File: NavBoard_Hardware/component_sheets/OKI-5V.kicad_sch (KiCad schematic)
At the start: 4 parts

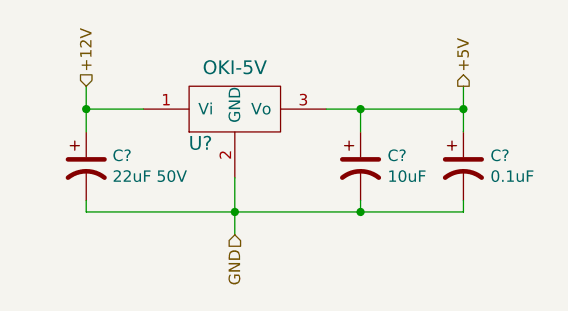
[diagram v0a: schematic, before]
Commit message: Created adapter symbols and footprints
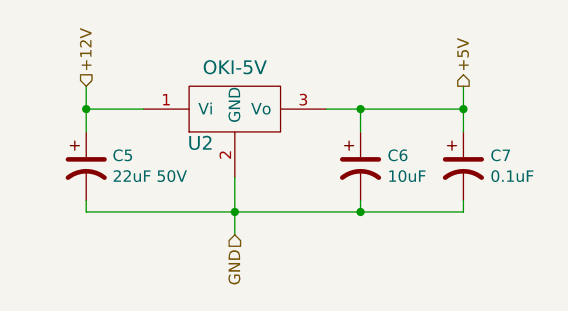
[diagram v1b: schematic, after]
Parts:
- gave numbers to parts that had none: 4
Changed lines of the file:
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@@
   (symbol (lib_id "Device:C_Polarized_US") (at 127.635 97.155 0) (unit 1)
     (in_bom yes) (on_board yes)
-    (property "Reference" "C?" (id 0) (at 130.556 95.9866 0)
+    (property "Reference" "C5" (id 0) (at 130.556 95.9866 0)
       (effects (font (size 1.27 1.27)) (justify left))
     )
@@
   (symbol (lib_id "Device:C_Polarized_US") (at 158.115 97.155 0) (unit 1)
     (in_bom yes) (on_board yes)
-    (property "Reference" "C?" (id 0) (at 161.1122 95.9866 0)
+    (property "Reference" "C6" (id 0) (at 161.1122 95.9866 0)
       (effects (font (size 1.27 1.27)) (justify left))
     )
@@
   (symbol (lib_id "Device:C_Polarized_US") (at 169.545 97.155 0) (unit 1)
     (in_bom yes) (on_board yes)
-    (property "Reference" "C?" (id 0) (at 172.5422 95.9866 0)
+    (property "Reference" "C7" (id 0) (at 172.5422 95.9866 0)
       (effects (font (size 1.27 1.27)) (justify left))
     )
@@
   (symbol (lib_id "MRDT_Devices:OKI") (at 139.065 93.345 0) (unit 1)
     (in_bom yes) (on_board yes)
-    (property "Reference" "U?" (id 0) (at 140.335 94.615 0)
+    (property "Reference" "U2" (id 0) (at 140.335 94.615 0)
       (effects (font (size 1.524 1.524)))
     )

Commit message: Added connectors, cleaned up file directory
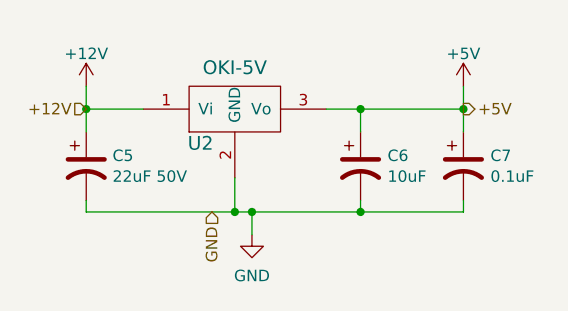
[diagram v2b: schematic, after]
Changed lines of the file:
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@@
     (comment 2 "Provides Stable 5V From 12V Input")
+  )
+  (junction (at 146.05 102.235) (diameter 0) (color 0 0 0 0)
   )
   (junction (at 158.115 102.235) (diameter 0) (color 0 0 0 0)
@@
   )
   (junction (at 169.545 90.805) (diameter 0) (color 0 0 0 0)
+  )
+  (wire (pts (xy 146.05 102.235) (xy 158.115 102.235))
+    (stroke (width 0) (type default) (color 0 0 0 0))
   )
   (wire (pts (xy 127.635 88.265) (xy 127.635 90.805))
@@
     (stroke (width 0) (type default) (color 0 0 0 0))
   )
-  (wire (pts (xy 144.145 102.235) (xy 158.115 102.235))
+  (wire (pts (xy 144.145 102.235) (xy 146.05 102.235))
     (stroke (width 0) (type default) (color 0 0 0 0))
   )
-  (wire (pts (xy 144.145 102.235) (xy 144.145 104.775))
+  (wire (pts (xy 146.05 102.235) (xy 146.05 104.775))
     (stroke (width 0) (type default) (color 0 0 0 0))
   )
@@
     (stroke (width 0) (type default) (color 0 0 0 0))
   )
-  (hierarchical_label "GND" (shape input) (at 144.145 104.775 270)
+  (hierarchical_label "GND" (shape input) (at 141.605 102.235 270)
     (effects (font (size 1.27 1.27)) (justify right))
   )
-  (hierarchical_label "+5V" (shape output) (at 169.545 88.265 90)
+  (hierarchical_label "+5V" (shape output) (at 169.545 90.805 0)
     (effects (font (size 1.27 1.27)) (justify left))
   )
-  (hierarchical_label "+12V" (shape input) (at 127.635 88.265 90)
-    (effects (font (size 1.27 1.27)) (justify left))
+  (hierarchical_label "+12V" (shape input) (at 127.635 90.805 180)
+    (effects (font (size 1.27 1.27)) (justify right))
   )
   (symbol (lib_id "Device:C_Polarized_US") (at 127.635 97.155 0) (unit 1)
@@
     (pin "1")
     (pin "2")
+  )
+  (symbol (lib_id "power:+5V") (at 169.545 88.265 0) (unit 1)
+    (in_bom yes) (on_board yes) (fields_autoplaced)
+    (property "Reference" "#PWR?" (id 0) (at 169.545 92.075 0)
+      (effects (font (size 1.27 1.27)) hide)
+    )
+    (property "Value" "+5V" (id 1) (at 169.545 84.6605 0))
+    (property "Footprint" "" (id 2) (at 169.545 88.265 0)
+      (effects (font (size 1.27 1.27)) hide)
+    )
+    (property "Datasheet" "" (id 3) (at 169.545 88.265 0)
+      (effects (font (size 1.27 1.27)) hide)
+    )
+    (pin "1")
+  )
+  (symbol (lib_id "power:+12V") (at 127.635 88.265 0) (unit 1)
+    (in_bom yes) (on_board yes) (fields_autoplaced)
+    (property "Reference" "#PWR?" (id 0) (at 127.635 92.075 0)
+      (effects (font (size 1.27 1.27)) hide)
+    )
+    (property "Value" "+12V" (id 1) (at 127.635 84.6605 0))
+    (property "Footprint" "" (id 2) (at 127.635 88.265 0)
+      (effects (font (size 1.27 1.27)) hide)
+    )
+    (property "Datasheet" "" (id 3) (at 127.635 88.265 0)
+      (effects (font (size 1.27 1.27)) hide)
+    )
+    (pin "1")
   )
   (symbol (lib_id "Device:C_Polarized_US") (at 169.545 97.155 0) (unit 1)
@@
     (pin "3")
   )
+  (symbol (lib_id "power:GND") (at 146.05 104.775 0) (unit 1)
+    (in_bom yes) (on_board yes) (fields_autoplaced)
+    (property "Reference" "#PWR?" (id 0) (at 146.05 111.125 0)
+      (effects (font (size 1.27 1.27)) hide)
+    )
+    (property "Value" "GND" (id 1) (at 146.05 109.3375 0))
+    (property "Footprint" "" (id 2) (at 146.05 104.775 0)
+      (effects (font (size 1.27 1.27)) hide)
+    )
+    (property "Datasheet" "" (id 3) (at 146.05 104.775 0)
+      (effects (font (size 1.27 1.27)) hide)
+    )
+    (pin "1")
+  )
 )

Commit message: Placed OKI SMD components, aligned ethernet pins
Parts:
- C5: footprint Capacitor_THT:CP_Radial_D6.3mm_P2.50mm -> Capacitor_SMD:C_1206_3216Metric_Pad1.33x1.80mm_HandSolder
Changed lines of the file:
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@@
       (effects (font (size 1.27 1.27)) (justify left))
     )
-    (property "Footprint" "Capacitor_THT:CP_Radial_D6.3mm_P2.50mm" (id 2) (at 127.635 97.155 0)
+    (property "Footprint" "Capacitor_SMD:C_1206_3216Metric_Pad1.33x1.80mm_HandSolder" (id 2) (at 127.635 97.155 0)
       (effects (font (size 1.27 1.27)) hide)
     )

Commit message: Annotated schematic pages
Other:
- company: Missouri S&T Mars Rover Design Team -> Thomas Francois, Missouri S&T Mars Rover Design Team
- title: OKI 5V Voltage Regulator -> MRDT NavBoard
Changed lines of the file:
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@@
   (paper "A4")
   (title_block
-    (title "OKI 5V Voltage Regulator")
-    (company "Missouri S&T Mars Rover Design Team")
+    (title "MRDT NavBoard")
+    (rev "1, 2023")
+    (company "Thomas Francois, Missouri S&T Mars Rover Design Team")
     (comment 1 "OKI 5V Voltage Regulator")
-    (comment 2 "Provides Stable 5V From 12V Input")
+    (comment 2 "Provides stable 5V from 12V input")
   )
   (junction (at 146.05 102.235) (diameter 0) (color 0 0 0 0)

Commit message: Rearranged schematic
I realize now that this is a dumb idea...
Going to redesign the board so the teensy just sits on top
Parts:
- renumbered C5 to C?, C6 to C?, C7 to C?, U2 to U?
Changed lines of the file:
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@@
     (effects (font (size 1.27 1.27)) (justify right))
   )
-  (symbol (lib_id "Device:C_Polarized_US") (at 127.635 97.155 0) (unit 1)
+  (symbol (lib_id "Device:C_Polarized_US") (at 127.635 97.155 0)
     (in_bom yes) (on_board yes)
-    (property "Reference" "C5" (id 0) (at 130.556 95.9866 0)
+    (property "Reference" "C?" (id 0) (at 130.556 95.9866 0)
       (effects (font (size 1.27 1.27)) (justify left))
     )
@@
     (pin "2")
   )
-  (symbol (lib_id "Device:C_Polarized_US") (at 158.115 97.155 0) (unit 1)
+  (symbol (lib_id "Device:C_Polarized_US") (at 158.115 97.155 0)
     (in_bom yes) (on_board yes)
-    (property "Reference" "C6" (id 0) (at 161.1122 95.9866 0)
+    (property "Reference" "C?" (id 0) (at 161.1122 95.9866 0)
       (effects (font (size 1.27 1.27)) (justify left))
     )
@@
     (pin "2")
   )
-  (symbol (lib_id "power:+5V") (at 169.545 88.265 0) (unit 1)
+  (symbol (lib_id "power:+5V") (at 169.545 88.265 0)
     (in_bom yes) (on_board yes) (fields_autoplaced)
-    (property "Reference" "#PWR011" (id 0) (at 169.545 92.075 0)
+    (property "Reference" "#PWR?" (id 0) (at 169.545 92.075 0)
       (effects (font (size 1.27 1.27)) hide)
     )
@@
     (pin "1")
   )
-  (symbol (lib_id "power:+12V") (at 127.635 88.265 0) (unit 1)
+  (symbol (lib_id "power:+12V") (at 127.635 88.265 0)
     (in_bom yes) (on_board yes) (fields_autoplaced)
-    (property "Reference" "#PWR010" (id 0) (at 127.635 92.075 0)
+    (property "Reference" "#PWR?" (id 0) (at 127.635 92.075 0)
       (effects (font (size 1.27 1.27)) hide)
     )
@@
     (pin "1")
   )
-  (symbol (lib_id "Device:C_Polarized_US") (at 169.545 97.155 0) (unit 1)
+  (symbol (lib_id "Device:C_Polarized_US") (at 169.545 97.155 0)
     (in_bom yes) (on_board yes)
-    (property "Reference" "C7" (id 0) (at 172.5422 95.9866 0)
+    (property "Reference" "C?" (id 0) (at 172.5422 95.9866 0)
       (effects (font (size 1.27 1.27)) (justify left))
     )
@@
     (pin "2")
   )
-  (symbol (lib_id "MRDT_Devices:OKI") (at 139.065 93.345 0) (unit 1)
+  (symbol (lib_id "MRDT_Devices:OKI") (at 139.065 93.345 0)
     (in_bom yes) (on_board yes)
-    (property "Reference" "U2" (id 0) (at 140.335 94.615 0)
+    (property "Reference" "U?" (id 0) (at 140.335 94.615 0)
       (effects (font (size 1.524 1.524)))
     )
@@
     (pin "3")
   )
-  (symbol (lib_id "power:GND") (at 146.05 104.775 0) (unit 1)
+  (symbol (lib_id "power:GND") (at 146.05 104.775 0)
     (in_bom yes) (on_board yes) (fields_autoplaced)
-    (property "Reference" "#PWR012" (id 0) (at 146.05 111.125 0)
+    (property "Reference" "#PWR?" (id 0) (at 146.05 111.125 0)
       (effects (font (size 1.27 1.27)) hide)
     )

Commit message: Decided on pcb layout
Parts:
- U?: footprint MRDT_Devices:OKI_Horizontal -> Converter_DCDC:Converter_DCDC_Murata_OKI-78SR_Vertical
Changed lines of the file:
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@@
     (effects (font (size 1.27 1.27)) (justify right))
   )
-  (symbol (lib_id "Device:C_Polarized_US") (at 127.635 97.155 0)
+  (symbol (lib_id "Device:C_Polarized_US") (at 127.635 97.155 0) (unit 1)
     (in_bom yes) (on_board yes)
     (property "Reference" "C?" (id 0) (at 130.556 95.9866 0)
@@
     (pin "2")
   )
-  (symbol (lib_id "Device:C_Polarized_US") (at 158.115 97.155 0)
+  (symbol (lib_id "Device:C_Polarized_US") (at 158.115 97.155 0) (unit 1)
     (in_bom yes) (on_board yes)
     (property "Reference" "C?" (id 0) (at 161.1122 95.9866 0)
@@
     (pin "2")
   )
-  (symbol (lib_id "power:+5V") (at 169.545 88.265 0)
+  (symbol (lib_id "power:+5V") (at 169.545 88.265 0) (unit 1)
     (in_bom yes) (on_board yes) (fields_autoplaced)
-    (property "Reference" "#PWR?" (id 0) (at 169.545 92.075 0)
+    (property "Reference" "#PWR0123" (id 0) (at 169.545 92.075 0)
       (effects (font (size 1.27 1.27)) hide)
     )
@@
     (pin "1")
   )
-  (symbol (lib_id "power:+12V") (at 127.635 88.265 0)
+  (symbol (lib_id "power:+12V") (at 127.635 88.265 0) (unit 1)
     (in_bom yes) (on_board yes) (fields_autoplaced)
-    (property "Reference" "#PWR?" (id 0) (at 127.635 92.075 0)
+    (property "Reference" "#PWR0122" (id 0) (at 127.635 92.075 0)
       (effects (font (size 1.27 1.27)) hide)
     )
@@
     (pin "1")
   )
-  (symbol (lib_id "Device:C_Polarized_US") (at 169.545 97.155 0)
+  (symbol (lib_id "Device:C_Polarized_US") (at 169.545 97.155 0) (unit 1)
     (in_bom yes) (on_board yes)
     (property "Reference" "C?" (id 0) (at 172.5422 95.9866 0)
@@
     (pin "2")
   )
-  (symbol (lib_id "MRDT_Devices:OKI") (at 139.065 93.345 0)
+  (symbol (lib_id "MRDT_Devices:OKI") (at 139.065 93.345 0) (unit 1)
     (in_bom yes) (on_board yes)
     (property "Reference" "U?" (id 0) (at 140.335 94.615 0)
@@
       (effects (font (size 1.524 1.524)))
     )
-    (property "Footprint" "MRDT_Devices:OKI_Horizontal" (id 2) (at 133.985 95.885 0)
+    (property "Footprint" "Converter_DCDC:Converter_DCDC_Murata_OKI-78SR_Vertical" (id 2) (at 133.985 95.885 0)
       (effects (font (size 1.524 1.524)) hide)
     )
@@
     (pin "3")
   )
-  (symbol (lib_id "power:GND") (at 146.05 104.775 0)
+  (symbol (lib_id "power:GND") (at 146.05 104.775 0) (unit 1)
     (in_bom yes) (on_board yes) (fields_autoplaced)
-    (property "Reference" "#PWR?" (id 0) (at 146.05 111.125 0)
+    (property "Reference" "#PWR0121" (id 0) (at 146.05 111.125 0)
       (effects (font (size 1.27 1.27)) hide)
     )

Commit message: Realized this could all fit on a single board
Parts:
- U3: renamed from U?; footprint Converter_DCDC:Converter_DCDC_Murata_OKI-78SR_Vertical -> Nav_Board:OKI_Vertical_TSR
- gave numbers to parts that had none: 3
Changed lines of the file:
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@@
   (symbol (lib_id "Device:C_Polarized_US") (at 127.635 97.155 0) (unit 1)
     (in_bom yes) (on_board yes)
-    (property "Reference" "C?" (id 0) (at 130.556 95.9866 0)
+    (property "Reference" "C5" (id 0) (at 130.556 95.9866 0)
       (effects (font (size 1.27 1.27)) (justify left))
     )
@@
   (symbol (lib_id "Device:C_Polarized_US") (at 158.115 97.155 0) (unit 1)
     (in_bom yes) (on_board yes)
-    (property "Reference" "C?" (id 0) (at 161.1122 95.9866 0)
+    (property "Reference" "C6" (id 0) (at 161.1122 95.9866 0)
       (effects (font (size 1.27 1.27)) (justify left))
     )
@@
   (symbol (lib_id "power:+5V") (at 169.545 88.265 0) (unit 1)
     (in_bom yes) (on_board yes) (fields_autoplaced)
-    (property "Reference" "#PWR0123" (id 0) (at 169.545 92.075 0)
+    (property "Reference" "#PWR022" (id 0) (at 169.545 92.075 0)
       (effects (font (size 1.27 1.27)) hide)
     )
@@
   (symbol (lib_id "power:+12V") (at 127.635 88.265 0) (unit 1)
     (in_bom yes) (on_board yes) (fields_autoplaced)
-    (property "Reference" "#PWR0122" (id 0) (at 127.635 92.075 0)
+    (property "Reference" "#PWR021" (id 0) (at 127.635 92.075 0)
       (effects (font (size 1.27 1.27)) hide)
     )
@@
   (symbol (lib_id "Device:C_Polarized_US") (at 169.545 97.155 0) (unit 1)
     (in_bom yes) (on_board yes)
-    (property "Reference" "C?" (id 0) (at 172.5422 95.9866 0)
+    (property "Reference" "C7" (id 0) (at 172.5422 95.9866 0)
       (effects (font (size 1.27 1.27)) (justify left))
     )
@@
   (symbol (lib_id "MRDT_Devices:OKI") (at 139.065 93.345 0) (unit 1)
     (in_bom yes) (on_board yes)
-    (property "Reference" "U?" (id 0) (at 140.335 94.615 0)
+    (property "Reference" "U3" (id 0) (at 140.335 94.615 0)
       (effects (font (size 1.524 1.524)))
     )
@@
       (effects (font (size 1.524 1.524)))
     )
-    (property "Footprint" "Converter_DCDC:Converter_DCDC_Murata_OKI-78SR_Vertical" (id 2) (at 133.985 95.885 0)
+    (property "Footprint" "Nav_Board:OKI_Vertical_TSR" (id 2) (at 133.985 95.885 0)
       (effects (font (size 1.524 1.524)) hide)
     )
@@
   (symbol (lib_id "power:GND") (at 146.05 104.775 0) (unit 1)
     (in_bom yes) (on_board yes) (fields_autoplaced)
-    (property "Reference" "#PWR0121" (id 0) (at 146.05 111.125 0)
+    (property "Reference" "#PWR023" (id 0) (at 146.05 111.125 0)
       (effects (font (size 1.27 1.27)) hide)
     )
